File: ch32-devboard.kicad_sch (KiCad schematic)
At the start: 19 parts, among them J1 Conn_01x10_Pin, J2 Conn_01x05_Pin, J3 Conn_01x10_Pin, J4 USB_C_Receptacle_USB2.0_16P, J5 Conn_01x03_Socket, SW1 CK_KMS2xxG, U1 AP2112K-3.3

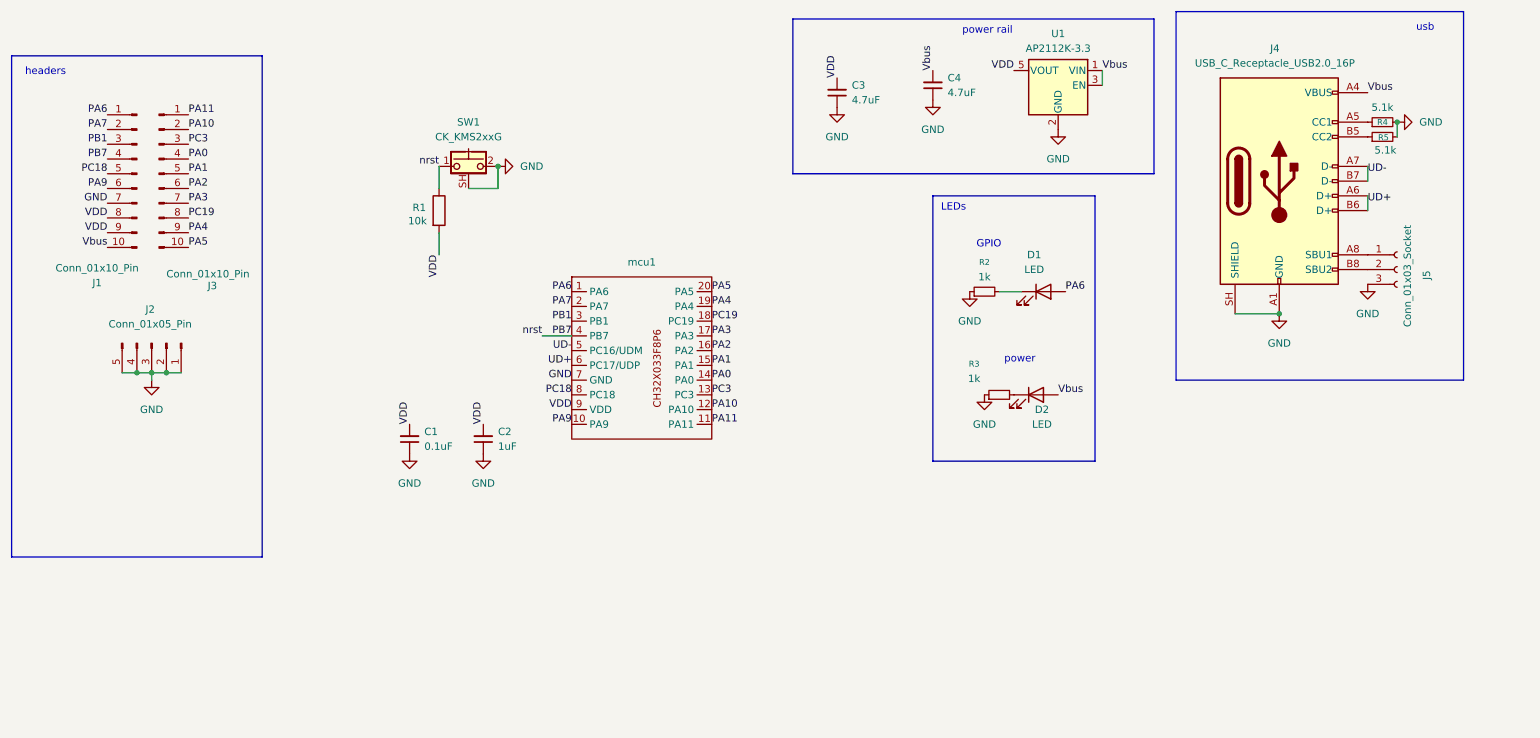
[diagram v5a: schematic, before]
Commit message: boot button, add drill data to exports, change usb C footprint
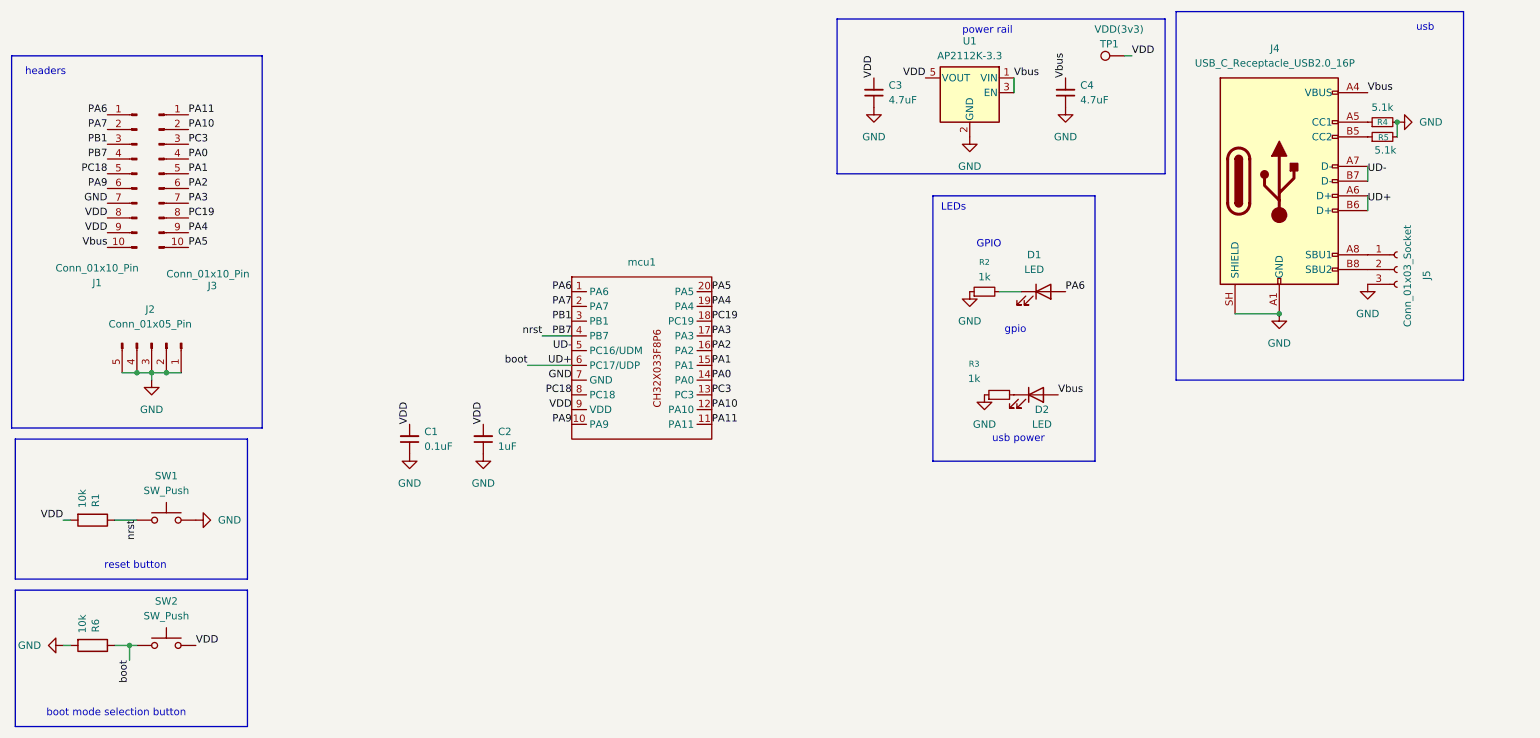
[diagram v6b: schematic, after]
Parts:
- removed SW1: CK_KMS2xxG, CH32-devBoard:smd-push-button-TS3425PA, symbol Switch:CK_KMS2xxG
- added R6: 10k, Resistor_SMD:R_0805_2012Metric_Pad1.20x1.40mm_HandSolder, symbol Device:R
- added SW1, SW2: SW_Push, ch32-devBoard-symbols:smd-push-button-TS3425PA, symbol Switch:SW_Push
- added TP1: VDD(3v3), TestPoint:TestPoint_Pad_1.0x1.0mm, symbol Connector:TestPoint
- J4: footprint Connector_USB:USB_C_Receptacle_XKB_U262-16XN-4BVC11 -> Connector_USB:USB_C_Receptacle_Palconn_UTC16-G
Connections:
- net GND: now also R6.2, SW1.2
- net PB7: now also SW1.1
- net UD+: now also R6.1, SW2.1
- net VDD: now also SW2.2, TP1.1
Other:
- note added: "boot mode selection button"
- note added: "gpio"
- note added: "reset button"
- note added: "usb power"
- note removed: "power"
- moved on the sheet: R1, U1
